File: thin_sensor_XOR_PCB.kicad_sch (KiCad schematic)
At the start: 38 parts, among them U1 CD4030BM96

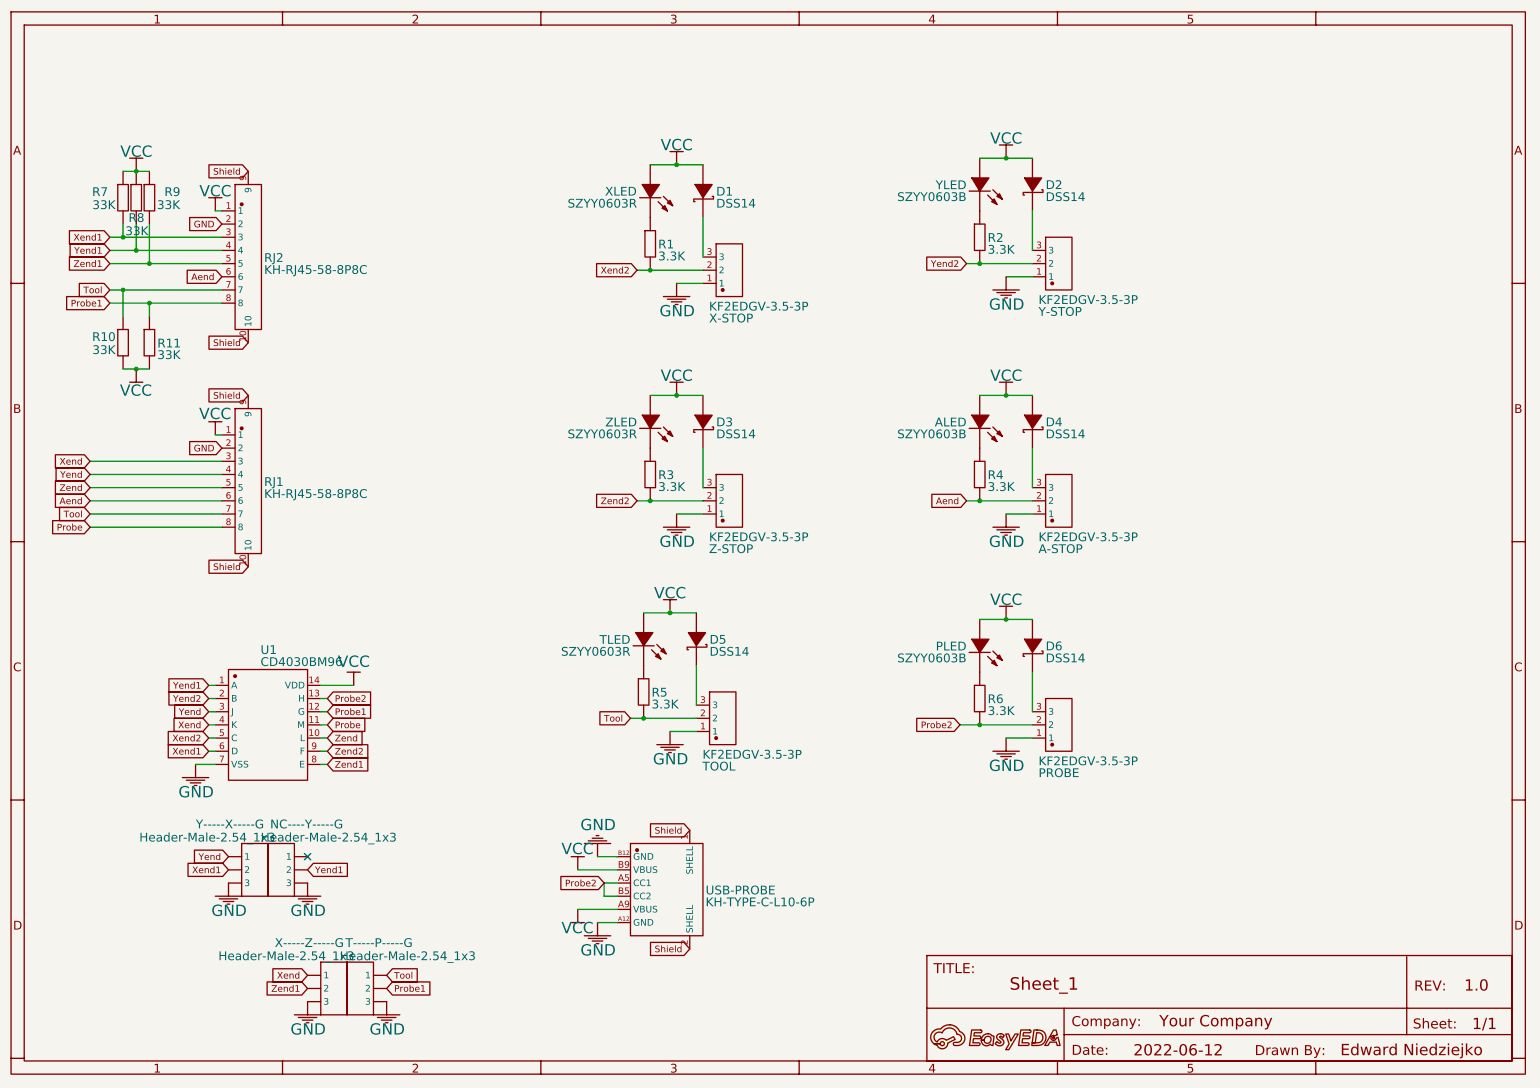
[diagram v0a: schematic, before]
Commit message: Removed jumpers and XOR combinations I don't need
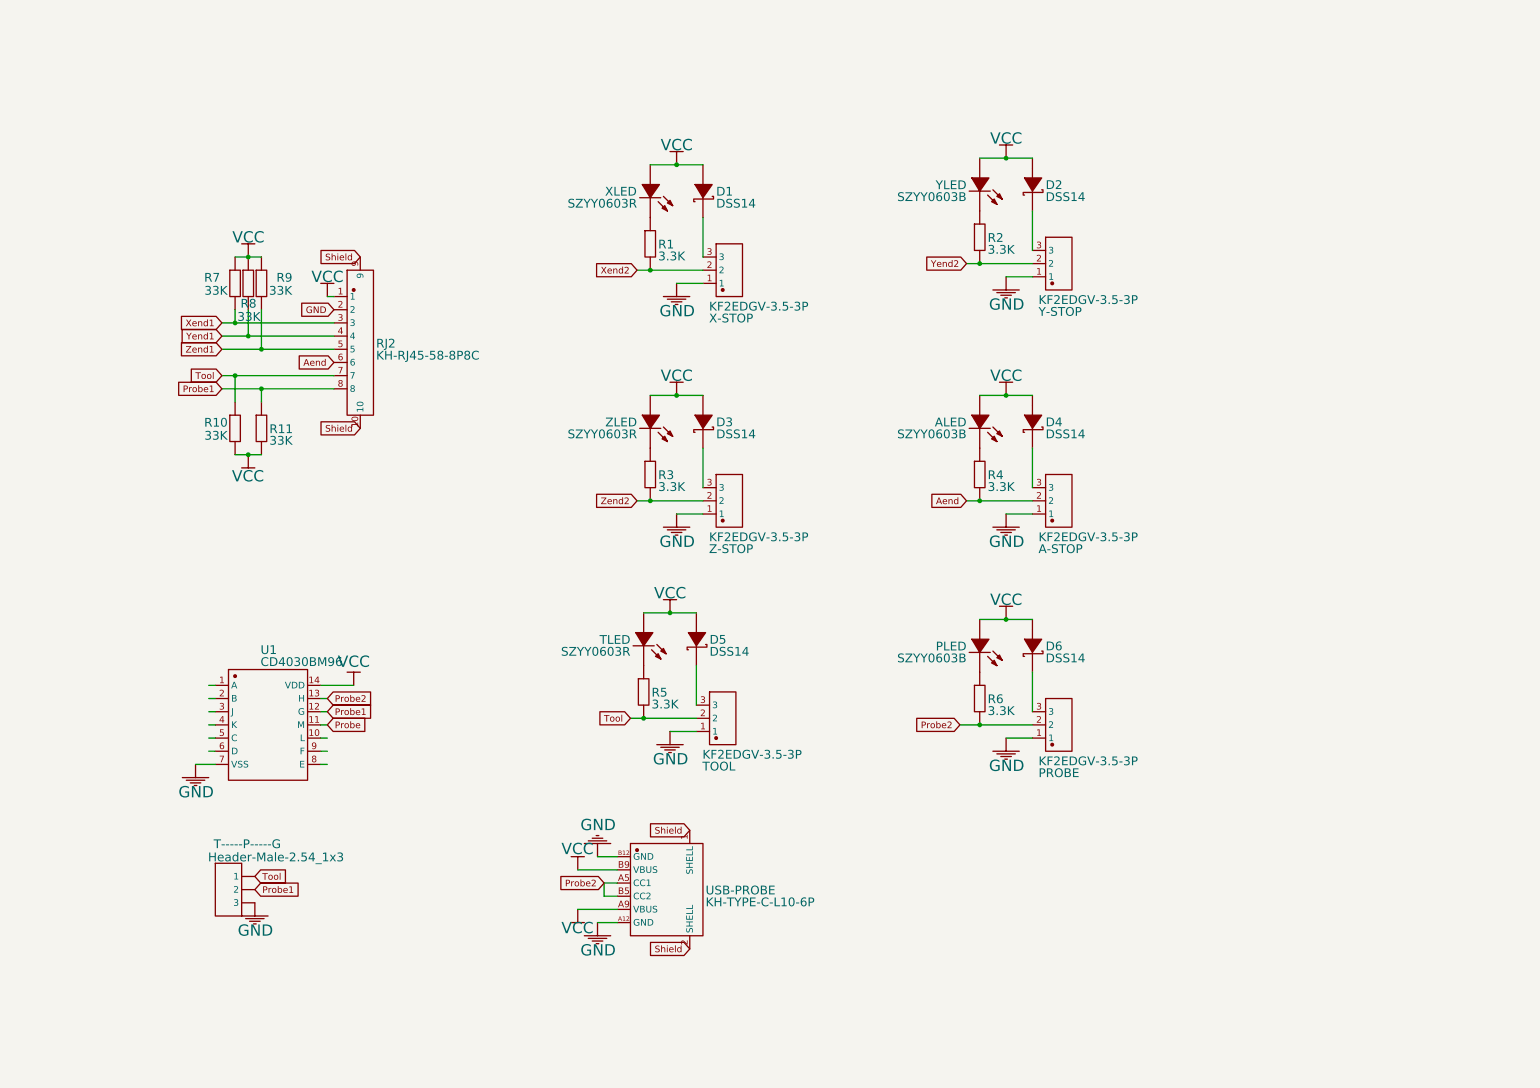
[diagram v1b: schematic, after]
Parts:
- removed A: A, symbol Unknown_0_-806
- removed NC----Y-----G: Header-Male-2.54_1x3, symbol Header-Male-2.54_1x3_1
- removed RJ1: KH-RJ45-58-8P8C, symbol KH-RJ45-58-8P8C
- removed X-----Z-----G: Header-Male-2.54_1x3, symbol Header-Male-2.54_1x3_3
- removed Y-----X-----G: Header-Male-2.54_1x3, symbol Header-Male-2.54_1x3
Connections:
- net Xend1: no longer U1.6 (D)
- net Xend2: no longer U1.5 (C)
- net Yend1: no longer U1.1 (A)
- net Yend2: no longer U1.2 (B)
- net Zend1: no longer U1.8 (E)
- net Zend2: no longer U1.9 (F)
- net Xend: no longer names the net of U1.4 (K)
- net Yend: no longer names the net of U1.3 (J)
- net Zend: no longer names the net of U1.10 (L)
- no-connect marks 1 -> 0
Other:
- moved on the sheet: R10, R11, R7, R8, R9, RJ2, T-----P-----G

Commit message: Added footprints, models etc
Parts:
- A-STOP, PROBE, TOOL, X-STOP, Y-STOP, Z-STOP: value KF2EDGV-3.5-3P -> Molex Microfit 3.0 43650-0315; footprint (none) -> Connector_Molex:Molex_Micro-Fit_3.0_43650-0315_1x03_P3.00mm_Vertical
- ALED, PLED, TLED, XLED, YLED, ZLED: footprint (none) -> LED_SMD:LED_0201_0603Metric_Pad0.64x0.40mm_HandSolder
- D1, D2, D3, D4, D5, D6: footprint (none) -> thin sensor pcb custom:SOD-123FL_L2.8-W1.8-LS3.7-RD
- R1, R10, R11, R2, R3, R4, R5, R6, R7, R8, R9: footprint (none) -> Resistor_SMD:R_0805_2012Metric_Pad1.20x1.40mm_HandSolder
- RJ2: footprint (none) -> thin sensor pcb custom:RJ45-TH_KH-RJ45-58-8P8C
- T-----P-----G: footprint (none) -> Connector_PinHeader_2.54mm:PinHeader_1x03_P2.54mm_Vertical
- U1: footprint (none) -> thin sensor pcb custom:SOIC-14_L8.7-W3.9-P1.27-LS6.0-BL
- USB-PROBE: footprint (none) -> thin sensor pcb custom:USB-C-TH_KH-TYPE-C-L10-6P

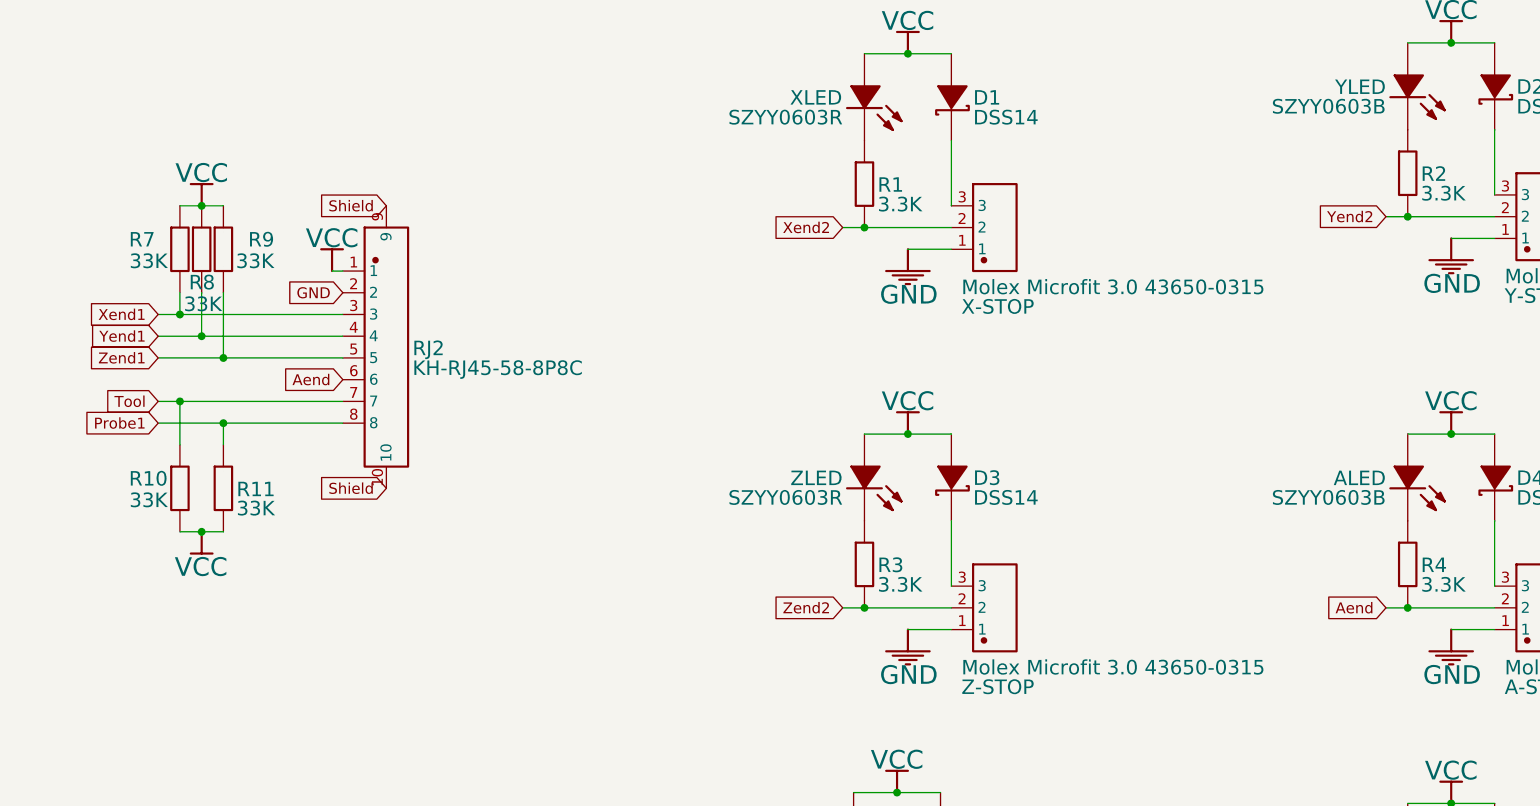
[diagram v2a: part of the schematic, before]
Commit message: Removed the correct RJ45 port this time
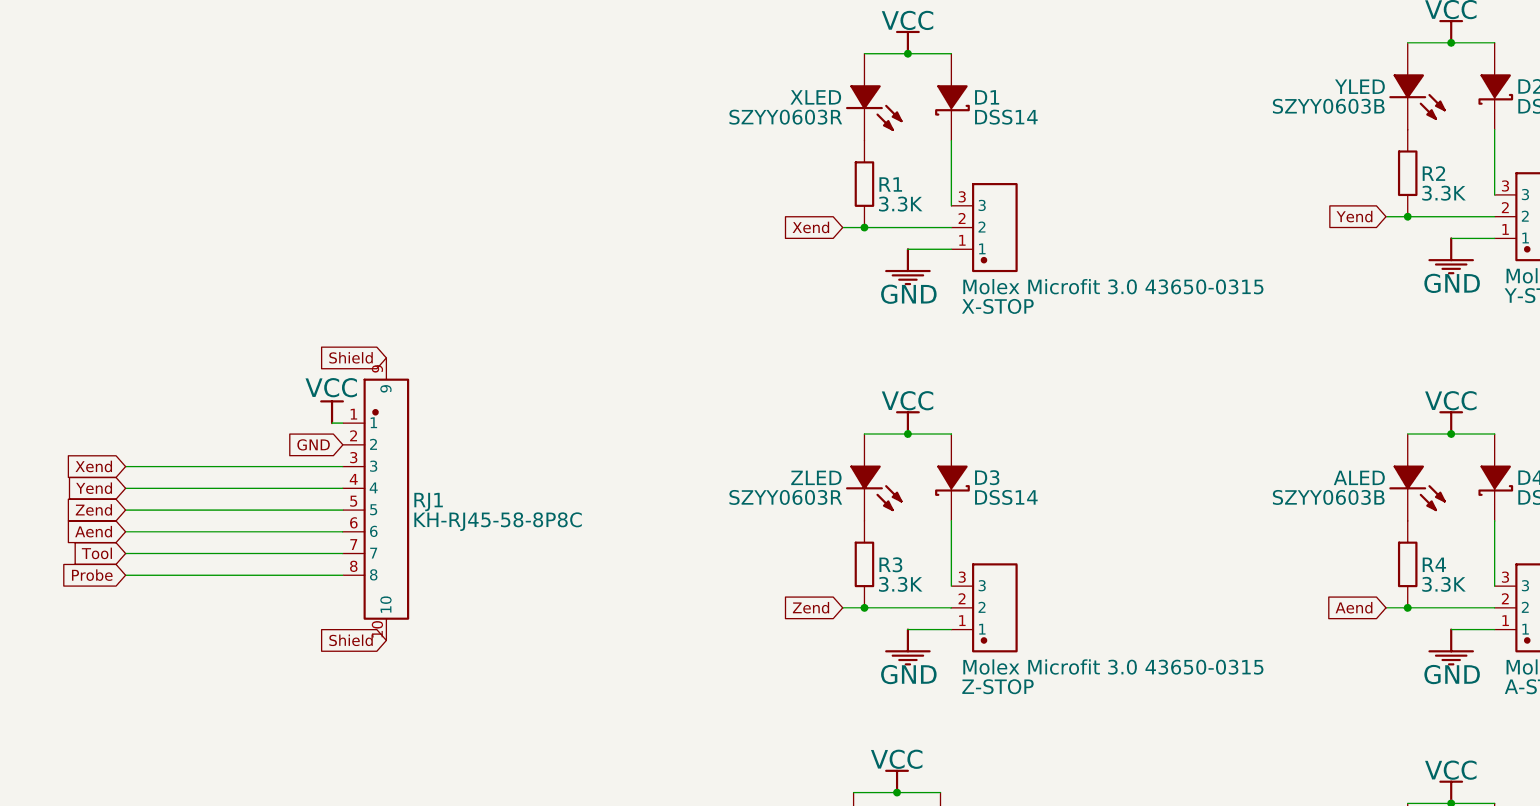
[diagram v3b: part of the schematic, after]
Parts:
- removed R10: 33K, Resistor_SMD:R_0805_2012Metric_Pad1.20x1.40mm_HandSolder, symbol RC0805JR-0733KL_3
- removed R11: 33K, Resistor_SMD:R_0805_2012Metric_Pad1.20x1.40mm_HandSolder, symbol RC0805JR-0733KL_2
- removed R7: 33K, Resistor_SMD:R_0805_2012Metric_Pad1.20x1.40mm_HandSolder, symbol RC0805JR-0733KL
- removed R8: 33K, Resistor_SMD:R_0805_2012Metric_Pad1.20x1.40mm_HandSolder, symbol RC0805JR-0733KL_1
- removed R9: 33K, Resistor_SMD:R_0805_2012Metric_Pad1.20x1.40mm_HandSolder, symbol RC0805JR-0733KL_4
- removed RJ2: KH-RJ45-58-8P8C, thin sensor pcb custom:RJ45-TH_KH-RJ45-58-8P8C, symbol KH-RJ45-58-8P8C_1
- added RJ1: KH-RJ45-58-8P8C, thin sensor pcb custom:RJ45-TH_KH-RJ45-58-8P8C, symbol KH-RJ45-58-8P8C
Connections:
- net Aend: now also RJ1.6
- net GND: now also RJ1.2
- net Probe: now also RJ1.8
- net Shield: now also RJ1.10, RJ1.9
- net Tool: now also RJ1.7
- net VCC: now also RJ1.1
- net Xend2 renamed Xend
- net Xend: now also RJ1.3
- net Yend2 renamed Yend
- net Yend: now also RJ1.4
- net Zend2 renamed Zend
- net Zend: now also RJ1.5

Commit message: Finished schematic and layout
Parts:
- added EHALT1, EHALTOUT1: Molex Microfit 3.0 436500215, thin sensor pcb custom:CONN-TH_436500215, symbol thin_{colon}sensor_xor_pcb_sym:436500215
- added PROBEINV1, TOOLOTINV1: Header-Male-2.54_1x3, Connector_PinHeader_2.54mm:PinHeader_1x03_P2.54mm_Vertical, symbol Header-Male-2.54_1x3_2
- added R7: 33K, thin sensor pcb custom:R0805, symbol thin_{colon}sensor_xor_pcb_sym:RC0805JR-0733KL
- A-STOP: footprint Connector_Molex:Molex_Micro-Fit_3.0_43650-0315_1x03_P3.00mm_Vertical -> thin sensor pcb custom:CONN-TH_436500315; symbol KF2EDGV-3.5-3P_1 -> thin_{colon}sensor_xor_pcb_sym:436500315; LCSC Part (none) -> C293546
- ALED: value SZYY0603B -> ~; footprint LED_SMD:LED_0201_0603Metric_Pad0.64x0.40mm_HandSolder -> thin sensor pcb custom:LED0805-RD_RED; symbol SZYY0603B_1 -> thin_{colon}sensor_xor_pcb_sym:HL-PSC-2012U36FC; BOM_Manufacturer yongyu(永裕光电) -> (none); BOM_Manufacturer Part SZYY0603B -> (none); BOM_Supplier Part C434421 -> (none); LCSC Part (none) -> C497949
- PLED: value SZYY0603B -> ~; footprint LED_SMD:LED_0201_0603Metric_Pad0.64x0.40mm_HandSolder -> thin sensor pcb custom:LED0805-RD_RED; symbol SZYY0603B_2 -> thin_{colon}sensor_xor_pcb_sym:HL-PSC-2012U36FC; BOM_Manufacturer yongyu(永裕光电) -> (none); BOM_Manufacturer Part SZYY0603B -> (none); BOM_Supplier Part C434421 -> (none); LCSC Part (none) -> C497949
- PROBE: footprint Connector_Molex:Molex_Micro-Fit_3.0_43650-0315_1x03_P3.00mm_Vertical -> thin sensor pcb custom:CONN-TH_436500315; symbol KF2EDGV-3.5-3P_5 -> thin_{colon}sensor_xor_pcb_sym:436500315; LCSC Part (none) -> C293546
- TLED: footprint LED_SMD:LED_0201_0603Metric_Pad0.64x0.40mm_HandSolder -> thin sensor pcb custom:LED0805-RD_RED; symbol SZYY0603R_2 -> thin_{colon}sensor_xor_pcb_sym:HL-PSC-2012U36FC; BOM_Manufacturer yongyu(永裕光电) -> (none); BOM_Manufacturer Part SZYY0603R -> (none); BOM_Supplier Part C434419 -> (none); LCSC Part (none) -> C497949
- TOOL: value Molex Microfit 3.0 43650-0315 -> Molex Microfit 3.0 43650-0415; footprint Connector_Molex:Molex_Micro-Fit_3.0_43650-0315_1x03_P3.00mm_Vertical -> thin sensor pcb custom:CONN-TH_436500415; symbol KF2EDGV-3.5-3P_2 -> thin_{colon}sensor_xor_pcb_sym:436500415; BOM_Supplier LCSC -> (none); BOM_Supplier Part C441322 -> (none); LCSC Part (none) -> C293547
- U1: symbol CD4030BM96 -> thin_{colon}sensor_xor_pcb_sym:CD4030BM96; LCSC Part (none) -> C44237
- X-STOP: footprint Connector_Molex:Molex_Micro-Fit_3.0_43650-0315_1x03_P3.00mm_Vertical -> thin sensor pcb custom:CONN-TH_436500315; symbol KF2EDGV-3.5-3P_3 -> thin_{colon}sensor_xor_pcb_sym:436500315; LCSC Part (none) -> C293546
- XLED: value SZYY0603R -> ~; footprint LED_SMD:LED_0201_0603Metric_Pad0.64x0.40mm_HandSolder -> thin sensor pcb custom:LED0805-RD_RED; symbol SZYY0603R -> thin_{colon}sensor_xor_pcb_sym:HL-PSC-2012U36FC; BOM_Manufacturer yongyu(永裕光电) -> (none); BOM_Manufacturer Part SZYY0603R -> (none); BOM_Supplier Part C434419 -> (none); LCSC Part (none) -> C497949
- Y-STOP: footprint Connector_Molex:Molex_Micro-Fit_3.0_43650-0315_1x03_P3.00mm_Vertical -> thin sensor pcb custom:CONN-TH_436500315; symbol KF2EDGV-3.5-3P -> thin_{colon}sensor_xor_pcb_sym:436500315; LCSC Part (none) -> C293546
- YLED: footprint LED_SMD:LED_0201_0603Metric_Pad0.64x0.40mm_HandSolder -> thin sensor pcb custom:LED0805-RD_RED; symbol SZYY0603B -> thin_{colon}sensor_xor_pcb_sym:HL-PSC-2012U36FC; BOM_Manufacturer yongyu(永裕光电) -> (none); BOM_Manufacturer Part SZYY0603B -> (none); BOM_Supplier Part C434421 -> (none); LCSC Part (none) -> C497949
- Z-STOP: footprint Connector_Molex:Molex_Micro-Fit_3.0_43650-0315_1x03_P3.00mm_Vertical -> thin sensor pcb custom:CONN-TH_436500315; symbol KF2EDGV-3.5-3P_4 -> thin_{colon}sensor_xor_pcb_sym:436500315; LCSC Part (none) -> C293546
- ZLED: value SZYY0603R -> ~; footprint LED_SMD:LED_0201_0603Metric_Pad0.64x0.40mm_HandSolder -> thin sensor pcb custom:LED0805-RD_RED; symbol SZYY0603R_1 -> thin_{colon}sensor_xor_pcb_sym:HL-PSC-2012U36FC; BOM_Manufacturer yongyu(永裕光电) -> (none); BOM_Manufacturer Part SZYY0603R -> (none); BOM_Supplier Part C434419 -> (none); LCSC Part (none) -> C497949
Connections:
- net GND: now also A-STOP.3, PROBE.3, TOOL.4, X-STOP.3, Y-STOP.3, Z-STOP.3, EHALT1.2, EHALTOUT1.2, PROBEINV1.3, TOOLOTINV1.3; no longer A-STOP.1, PROBE.1, TOOL.1, X-STOP.1, Y-STOP.1, Z-STOP.1
- net Tool: no longer T-----P-----G.1
- net VCC: now also ALED.2 (A), PLED.2 (A), T-----P-----G.1, TLED.2 (A), XLED.2 (A), YLED.2 (A), ZLED.2 (A), PROBEINV1.1, R7.1, TOOLOTINV1.1; no longer ALED.1 (+), PLED.1 (+), TLED.1 (+), XLED.1 (+), YLED.1 (+), ZLED.1 (+)
- net at R4.2: now also ALED.1 (C); no longer ALED.2 (-)
- net at D3.1 (K): now also Z-STOP.1; no longer Z-STOP.3
- net at D5.1 (K): now also TOOL.1; no longer TOOL.3
- net at R6.2: now also PLED.1 (C); no longer PLED.2 (-)
- net at D1.1 (K): now also X-STOP.1; no longer X-STOP.3
- net at R5.2: now also TLED.1 (C); no longer TLED.2 (-)
- net at D6.1 (K): now also PROBE.1; no longer PROBE.3
- net at R2.2: now also YLED.1 (C); no longer YLED.2 (-)
- net at R3.2: now also ZLED.1 (C); no longer ZLED.2 (-)
- net ExtEhaltInput: now reaches U1.1 (A)
- net ExtEhaltInput: now also EHALT1.1
- net EhaltOut: now reaches U1.10 (L)
- net EhaltOut: now also EHALTOUT1.1, R7.2
- net ExtEhaltInvert: now reaches U1.2 (B)
- net ExtEhaltInvert: now also T-----P-----G.2
- net ExtEhalt: now reaches U1.3 (J)
- net ExtEhalt: now also U1.8 (E)
- net ToolOvertravel: now reaches U1.4 (K)
- net ToolOvertravel: now also U1.9 (F)
- net ToolOvertravelInput: now reaches U1.5 (C)
- net ToolOvertravelInput: now also TOOL.3
- net ToolOverTravelInvert: now reaches U1.6 (D)
- net ToolOverTravelInvert: now also TOOLOTINV1.2
- net at D2.1 (K): now also Y-STOP.1; no longer Y-STOP.3
- net at D4.1 (K): now also A-STOP.1; no longer A-STOP.3
- net at R1.2: now also XLED.1 (C); no longer XLED.2 (-)
- net Probe1 renamed ProbeInvert
- net ProbeInvert: now also PROBEINV1.2; no longer T-----P-----G.2
- net Probe2 renamed ProbeInput
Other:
- moved on the sheet: A-STOP, ALED, D2, D4, D6, PLED, PROBE, R2, R4, R6, RJ1, TLED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
